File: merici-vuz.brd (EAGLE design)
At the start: 49.8 x 17.8 mm, 53 parts, among them IC1 MEGA328-PB, IC2 MCP73831, IC3 LE33, Q1 3,6864 MHz, Q4 TSM2302CX, T1 IRF7306

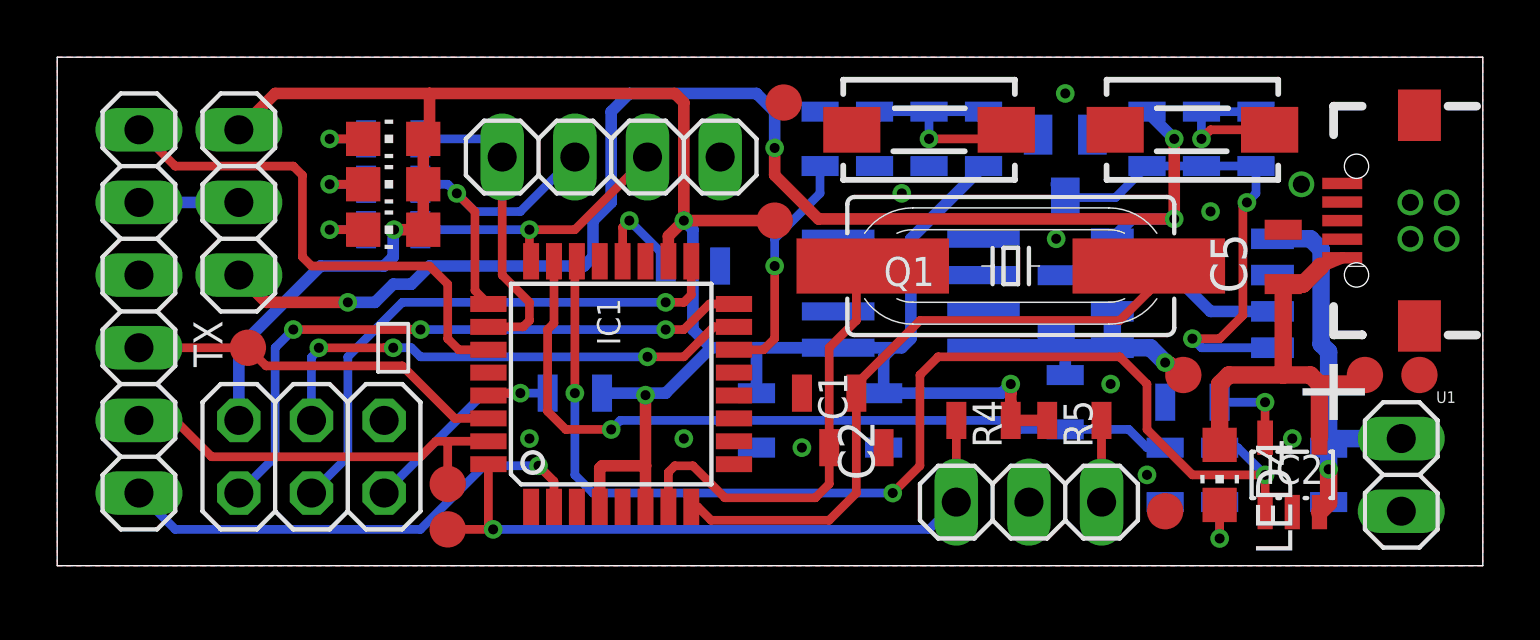
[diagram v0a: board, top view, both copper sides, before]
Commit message: BT takes power from VCC-BAT, not BAT-POS-VCC.
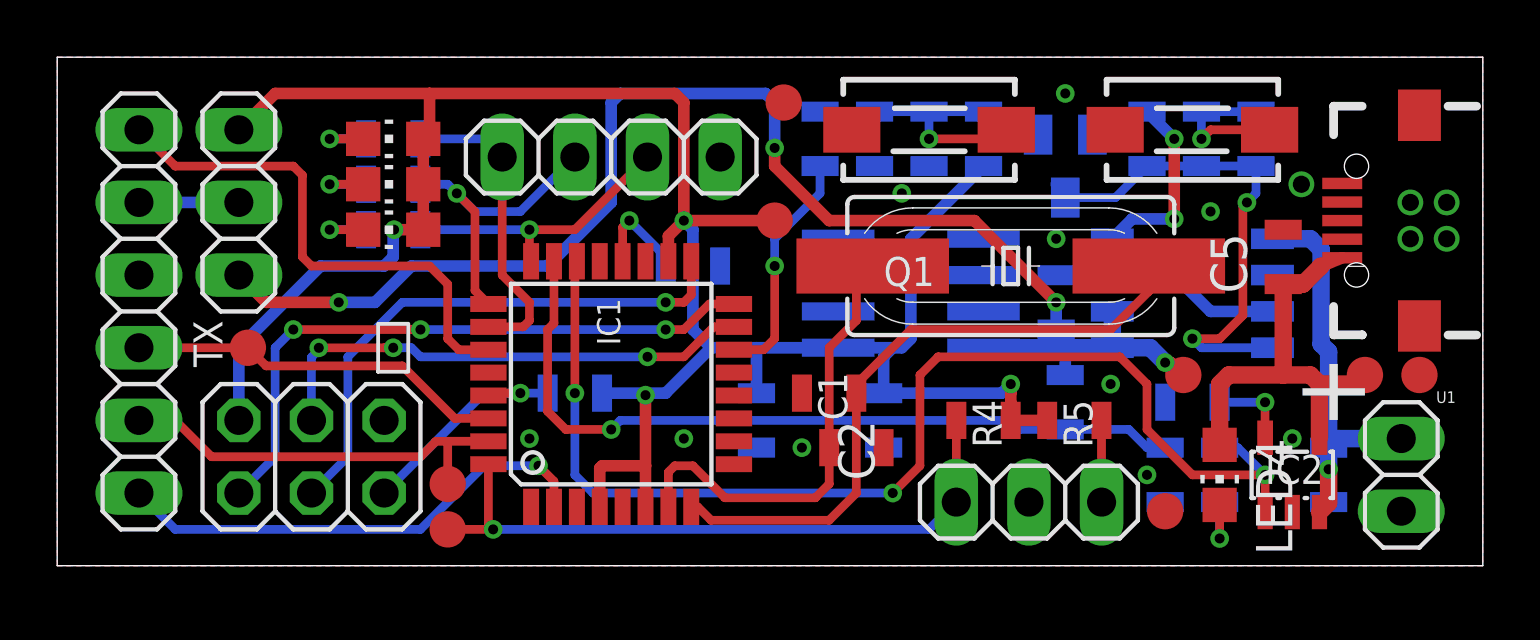
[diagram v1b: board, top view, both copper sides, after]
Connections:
- net BAT-POS-VCC: no longer CON-BT-POWER.3
- net VCC-BAT: now also CON-BT-POWER.3
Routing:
- net BAT-POS-VCC: track 55.8 -> 14.0 mm, vias 4 -> 2
- net VCC-BAT: track 10.5 -> 49.8 mm, vias 1 -> 4
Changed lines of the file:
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@@
 <grid distance="1.27" unitdist="mm" unit="mm" style="dots" multiple="2" display="no" altdistance="0.3175" altunitdist="mm" altunit="mm"/>
 <layers>
-<layer number="1" name="Top" color="3" fill="1" visible="no" active="yes"/>
+<layer number="1" name="Top" color="3" fill="1" visible="yes" active="yes"/>
 <layer number="2" name="Route2" color="1" fill="3" visible="no" active="no"/>
 <layer number="3" name="Route3" color="4" fill="3" visible="no" active="no"/>
@@
 <layer number="17" name="Pads" color="2" fill="1" visible="yes" active="yes"/>
 <layer number="18" name="Vias" color="2" fill="1" visible="yes" active="yes"/>
-<layer number="19" name="Unrouted" color="6" fill="1" visible="no" active="yes"/>
+<layer number="19" name="Unrouted" color="6" fill="1" visible="yes" active="yes"/>
 <layer number="20" name="Dimension" color="24" fill="1" visible="yes" active="yes"/>
-<layer number="21" name="tPlace" color="7" fill="1" visible="no" active="yes"/>
+<layer number="21" name="tPlace" color="7" fill="1" visible="yes" active="yes"/>
 <layer number="22" name="bPlace" color="7" fill="1" visible="yes" active="yes"/>
-<layer number="23" name="tOrigins" color="15" fill="1" visible="no" active="yes"/>
+<layer number="23" name="tOrigins" color="15" fill="1" visible="yes" active="yes"/>
 <layer number="24" name="bOrigins" color="15" fill="1" visible="yes" active="yes"/>
-<layer number="25" name="tNames" color="7" fill="1" visible="yes" active="yes"/>
-<layer number="26" name="bNames" color="7" fill="1" visible="yes" active="yes"/>
+<layer number="25" name="tNames" color="7" fill="1" visible="no" active="yes"/>
+<layer number="26" name="bNames" color="7" fill="1" visible="no" active="yes"/>
 <layer number="27" name="tValues" color="7" fill="1" visible="no" active="yes"/>
 <layer number="28" name="bValues" color="7" fill="1" visible="no" active="yes"/>
@@
 <layer number="44" name="Drills" color="7" fill="1" visible="no" active="yes"/>
 <layer number="45" name="Holes" color="7" fill="1" visible="no" active="yes"/>
-<layer number="46" name="Milling" color="3" fill="1" visible="no" active="yes"/>
+<layer number="46" name="Milling" color="3" fill="1" visible="yes" active="yes"/>
 <layer number="47" name="Measures" color="7" fill="1" visible="no" active="yes"/>
 <layer number="48" name="Document" color="7" fill="1" visible="no" active="yes"/>
-<layer number="49" name="Reference" color="7" fill="1" visible="no" active="yes"/>
+<layer number="49" name="Reference" color="7" fill="1" visible="yes" active="yes"/>
 <layer number="50" name="dxf" color="7" fill="1" visible="no" active="no"/>
-<layer number="51" name="tDocu" color="7" fill="1" visible="no" active="yes"/>
-<layer number="52" name="bDocu" color="7" fill="1" visible="no" active="yes"/>
+<layer number="51" name="tDocu" color="7" fill="1" visible="yes" active="yes"/>
+<layer number="52" name="bDocu" color="7" fill="1" visible="yes" active="yes"/>
 <layer number="53" name="tGND_GNDA" color="7" fill="9" visible="no" active="no"/>
 <layer number="54" name="bGND_GNDA" color="1" fill="9" visible="no" active="no"/>
@@
 <contactref element="C1" pad="2"/>
 <wire x1="38.1635" y1="10.4775" x2="38.1635" y2="9.5885" width="0.3048" layer="1"/>
-<wire x1="37.1475" y1="8.5725" x2="30.1625" y2="8.5725" width="0.3048" layer="1"/>
-<wire x1="30.1625" y1="8.5725" x2="27.94" y2="6.35" width="0.3048" layer="1"/>
-<wire x1="38.1635" y1="9.5885" x2="37.1475" y2="8.5725" width="0.3048" layer="1"/>
+<wire x1="36.83" y1="8.255" x2="29.845" y2="8.255" width="0.3048" layer="1"/>
+<wire x1="29.845" y1="8.255" x2="27.94" y2="6.35" width="0.3048" layer="1"/>
+<wire x1="38.1635" y1="9.5885" x2="36.83" y2="8.255" width="0.3048" layer="1"/>
 <wire x1="27.94" y1="6.35" x2="27.9425" y2="6.3475" width="0.3048" layer="1"/>
 <wire x1="27.9425" y1="6.3475" x2="27.9375" y2="6.0325" width="0.3048" layer="1"/>
@@
 <wire x1="38.9354" y1="7.1021" x2="39.37" y2="6.6675" width="0.4064" layer="1"/>
 <wire x1="35.2425" y1="6.665" x2="35.2425" y2="7.62" width="0.4064" layer="16"/>
+<contactref element="CON-BT-POWER" pad="3"/>
+<wire x1="25.0825" y1="16.1925" x2="25.0825" y2="14.605" width="0.4064" layer="16"/>
+<wire x1="24.765" y1="16.51" x2="25.0825" y2="16.1925" width="0.4064" layer="16"/>
+<wire x1="24.765" y1="16.51" x2="19.685" y2="16.51" width="0.4064" layer="16"/>
+<via x="25.0825" y="14.605" extent="1-16" drill="0.35"/>
+<wire x1="25.0825" y1="14.605" x2="25.0825" y2="13.97" width="0.4064" layer="1"/>
+<wire x1="25.0825" y1="13.97" x2="26.9875" y2="12.065" width="0.4064" layer="1"/>
+<wire x1="26.9875" y1="12.065" x2="32.0675" y2="12.065" width="0.4064" layer="1"/>
+<wire x1="19.685" y1="16.51" x2="19.3675" y2="16.1925" width="0.4064" layer="16"/>
+<wire x1="19.3675" y1="12.7" x2="17.145" y2="10.4775" width="0.4064" layer="16"/>
+<wire x1="19.3675" y1="16.1925" x2="19.3675" y2="12.7" width="0.4064" layer="16"/>
+<wire x1="12.3825" y1="10.4775" x2="11.1125" y2="9.2075" width="0.4064" layer="16"/>
+<wire x1="11.1125" y1="9.2075" x2="9.8425" y2="9.2075" width="0.4064" layer="16"/>
+<via x="9.8425" y="9.2075" extent="1-16" drill="0.35"/>
+<wire x1="9.8425" y1="9.2075" x2="7.3025" y2="9.2075" width="0.4064" layer="1"/>
+<wire x1="7.3025" y1="9.2075" x2="6.35" y2="10.16" width="0.4064" layer="1"/>
+<wire x1="17.145" y1="10.4775" x2="12.3825" y2="10.4775" width="0.4064" layer="16"/>
+<via x="34.925" y="9.2075" extent="1-16" drill="0.35"/>
+<wire x1="32.0675" y1="12.065" x2="34.925" y2="9.2075" width="0.4064" layer="1"/>
+<wire x1="34.925" y1="8.2575" x2="34.925" y2="9.2075" width="0.4064" layer="16"/>
 </signal>
 <signal name="BAT-SENSE">
@@
 </signal>
 <signal name="BAT-POS-VCC" class="2">
-<contactref element="CON-BT-POWER" pad="3"/>
 <contactref element="R10" pad="1"/>
 <contactref element="T1" pad="3"/>
@@
 <wire x1="37.58" y1="12.1225" x2="39.0525" y2="12.1225" width="0.4064" layer="16"/>
 <wire x1="36.8875" y1="10.16" x2="36.8875" y2="11.43" width="0.4064" layer="16"/>
-<wire x1="6.35" y1="10.16" x2="7.3025" y2="9.2075" width="0.4064" layer="1"/>
-<wire x1="7.3025" y1="9.2075" x2="10.16" y2="9.2075" width="0.4064" layer="1"/>
-<via x="10.16" y="9.2075" extent="1-16" drill="0.35"/>
-<wire x1="10.16" y1="9.2075" x2="11.1125" y2="9.2075" width="0.4064" layer="16"/>
-<wire x1="11.1125" y1="9.2075" x2="11.7475" y2="9.8425" width="0.4064" layer="16"/>
-<wire x1="11.7475" y1="9.8425" x2="12.3825" y2="9.8425" width="0.4064" layer="16"/>
-<wire x1="12.3825" y1="9.8425" x2="13.0175" y2="10.4775" width="0.4064" layer="16"/>
-<wire x1="13.0175" y1="10.4775" x2="18.415" y2="10.4775" width="0.4064" layer="16"/>
-<wire x1="18.415" y1="10.4775" x2="18.7325" y2="10.795" width="0.4064" layer="16"/>
-<wire x1="18.7325" y1="10.795" x2="18.7325" y2="12.065" width="0.4064" layer="16"/>
-<wire x1="18.7325" y1="12.065" x2="19.3675" y2="12.7" width="0.4064" layer="16"/>
-<wire x1="19.3675" y1="12.7" x2="19.3675" y2="15.875" width="0.4064" layer="16"/>
-<wire x1="19.3675" y1="15.875" x2="20.0025" y2="16.51" width="0.4064" layer="16"/>
-<wire x1="20.0025" y1="16.51" x2="24.4475" y2="16.51" width="0.4064" layer="16"/>
-<wire x1="24.4475" y1="16.51" x2="25.0825" y2="15.875" width="0.4064" layer="16"/>
-<wire x1="25.0825" y1="15.875" x2="25.0825" y2="14.605" width="0.4064" layer="16"/>
-<wire x1="26.6125" y1="12.1225" x2="25.0825" y2="13.6525" width="0.4064" layer="1"/>
-<via x="25.0825" y="14.605" extent="1-16" drill="0.35"/>
-<wire x1="39.0525" y1="12.1225" x2="26.6125" y2="12.1225" width="0.4064" layer="1"/>
-<wire x1="25.0825" y1="13.6525" x2="25.0825" y2="14.605" width="0.4064" layer="1"/>
 <wire x1="39.0525" y1="12.1225" x2="39.0525" y2="14.9225" width="0.4064" layer="1"/>
 <wire x1="38.1" y1="15.8725" x2="39.05" y2="14.9225" width="0.4064" layer="16"/>

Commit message: Add min. drill size to net classes.
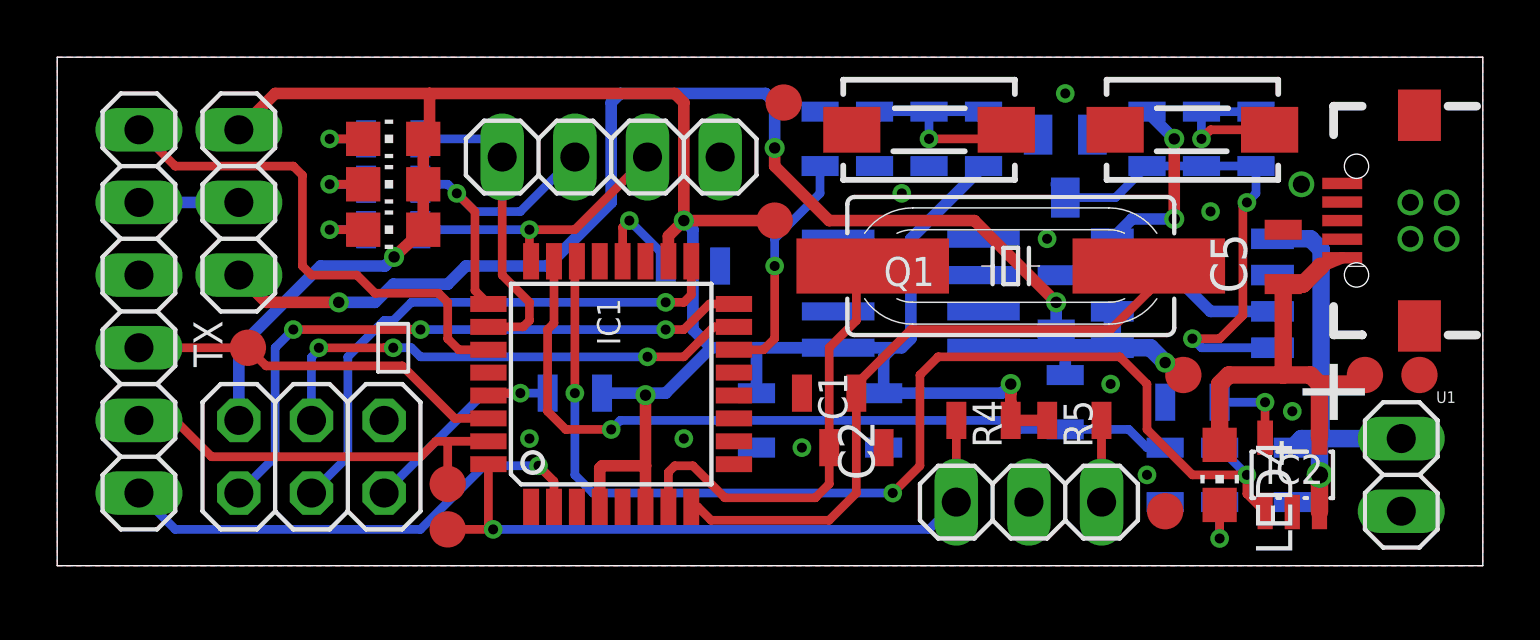
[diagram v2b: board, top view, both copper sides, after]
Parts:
- moved C11 1.27 mm to (43.2, 3.17)
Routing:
- net BAT-RAW-VCC: track 14.0 -> 15.0 mm
- net CHARGE-STAT: track 41.6 -> 40.6 mm
- net VCC: track 82.5 -> 81.9 mm

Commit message: Change shape of pins on pinheaders.
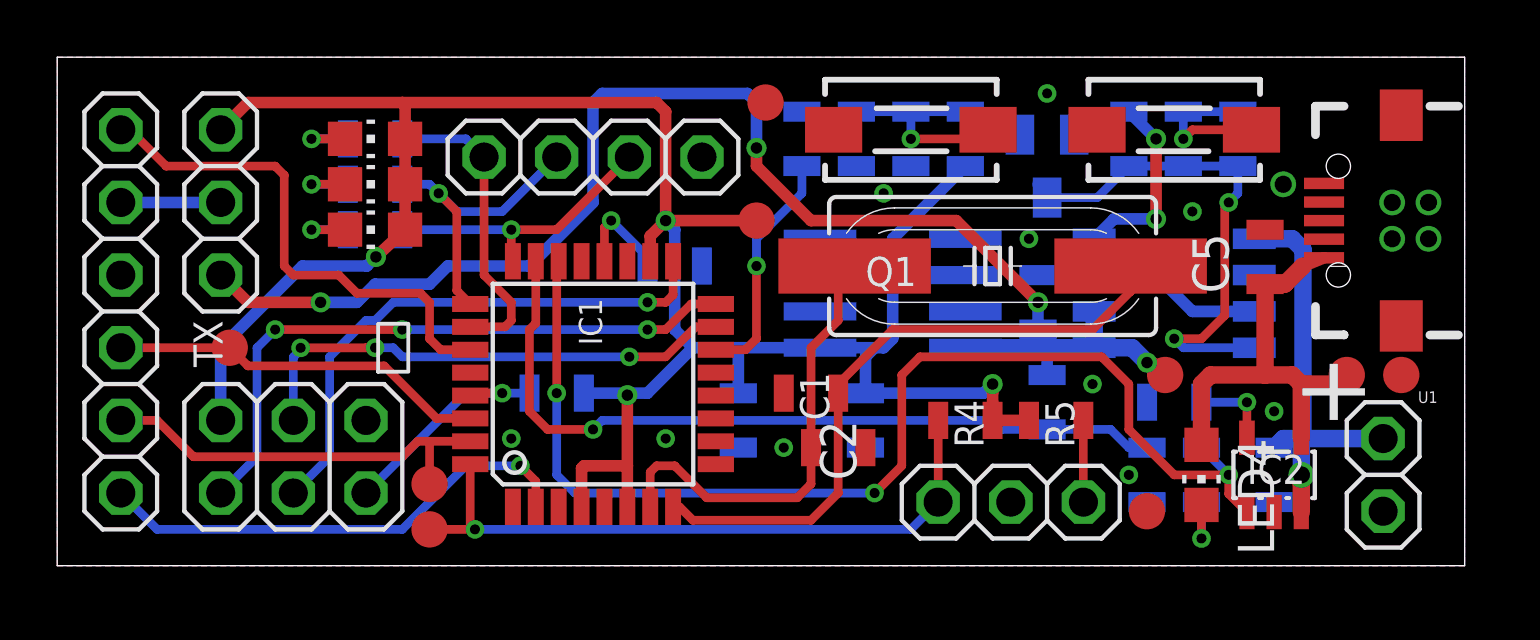
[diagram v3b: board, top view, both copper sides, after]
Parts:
- moved CON-BAT 0.64 mm to (46.4, 3.17)
- moved R11 0.64 mm to (39.4, 14.9)
- moved R5 0.64 mm to (34.9, 5.08)
- moved C1 0.64 mm to (26.4, 6.03)
- moved C2 0.64 mm to (27.3, 4.13)
- moved C3 0.64 mm to (23.8, 5.08)
- moved C4 0.64 mm to (21.6, 10.5)
- moved R12 0.64 mm to (29.8, 14.9)
- moved R15 0.64 mm to (26.0, 14.9)
- moved R6 0.64 mm to (17.5, 6.03)
- moved S-OFF 0.64 mm to (29.8, 15.2)
- moved TP8 0.64 mm to (6.03, 7.62)
- moved CON-BT 0.63 mm to (2.22, 8.89)
- moved CON-BT-POWER 0.63 mm to (5.71, 12.7)
- moved CON-PROG 0.63 mm to (8.26, 3.81)
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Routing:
- net VCC: track 81.9 -> 81.1 mm
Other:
- board size 49.8 x 17.8 mm -> 49.2 x 17.8 mm
